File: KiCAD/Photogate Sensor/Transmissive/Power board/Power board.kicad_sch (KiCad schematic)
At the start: 6 parts, among them J1 USB_B_Micro, J2 FFC Socket, J3 Conn_01x03_Socket, J4 DC Jack

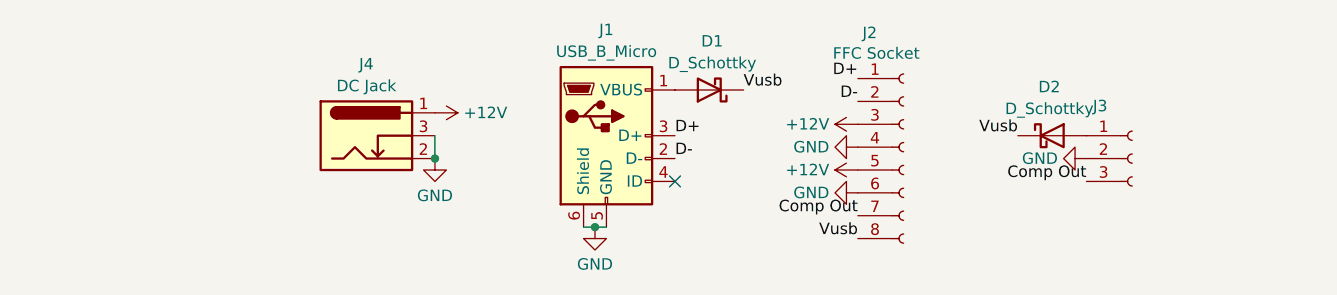
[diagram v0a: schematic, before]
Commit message: Place Gnds closer to data lines on FFC
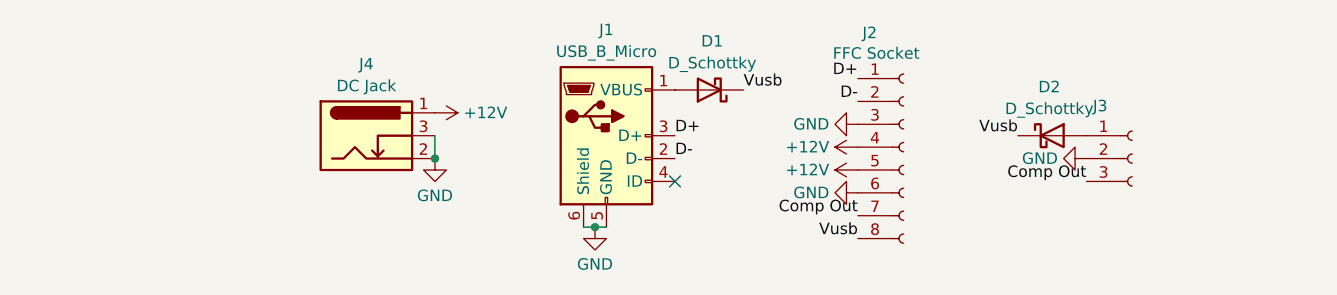
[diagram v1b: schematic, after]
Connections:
- net +12V: now also J2.4 (Pin_4); no longer J2.3 (Pin_3)
- net GND: now also J2.3 (Pin_3); no longer J2.4 (Pin_4)

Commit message: More ground optimizations
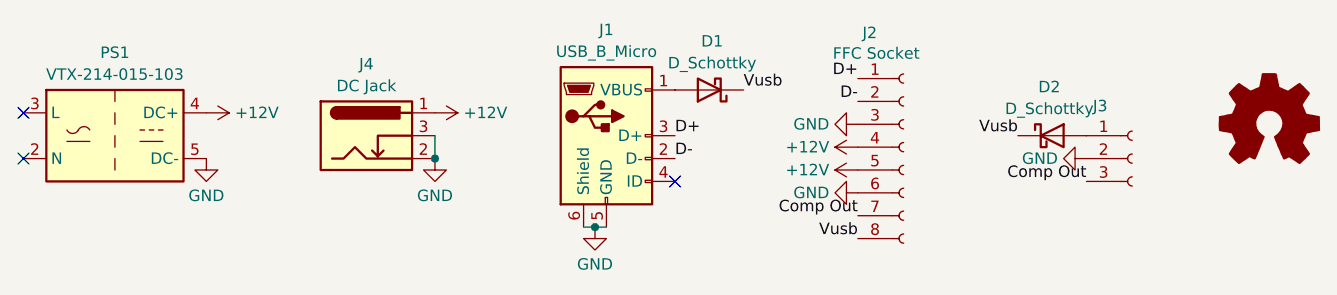
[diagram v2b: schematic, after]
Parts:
- added PS1: VTX-214-015-103, Converter_ACDC:Converter_ACDC_Vigortronix_VTX-214-015-1xx_THT, symbol Converter_ACDC:VTX-214-015-103
- added SYM1: Logo_Open_Hardware_Small, Custom:polarity, symbol Graphic:Logo_Open_Hardware_Small
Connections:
- net +12V: now also PS1.4 (DC+)
- net GND: now also PS1.5 (DC-)
- no-connect marks 1 -> 3
